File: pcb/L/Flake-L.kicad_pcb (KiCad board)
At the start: 2 copper layers, 139.2 x 114 mm, 62 parts, among them SW1 SW_Push, SW10 SW_Push, SW11 SW_Push, SW12 SW_Push, SW13 SW_Push, SW14 SW_Push, SW15 SW_Push, SW16 SW_Push, SW17 SW_Push, SW18 SW_Push, SW19 SW_Push, SW2 SW_Push, SW20 SW_Push, SW21 SW_Push, SW22 SW_Push, SW23 SW_Push, SW24 SW_Push, SW25 SW_Push, SW26 SW_Push, SW27 SW_Push, SW28 SW_Push, SW29 SW_Push, SW3 SW_Push, SW4 SW_Push, SW5 SW_Push, SW6 SW_Push, SW7 SW_Push, SW8 SW_Push, SW9 SW_Push, U1 XIAO-nRF52840-SMD

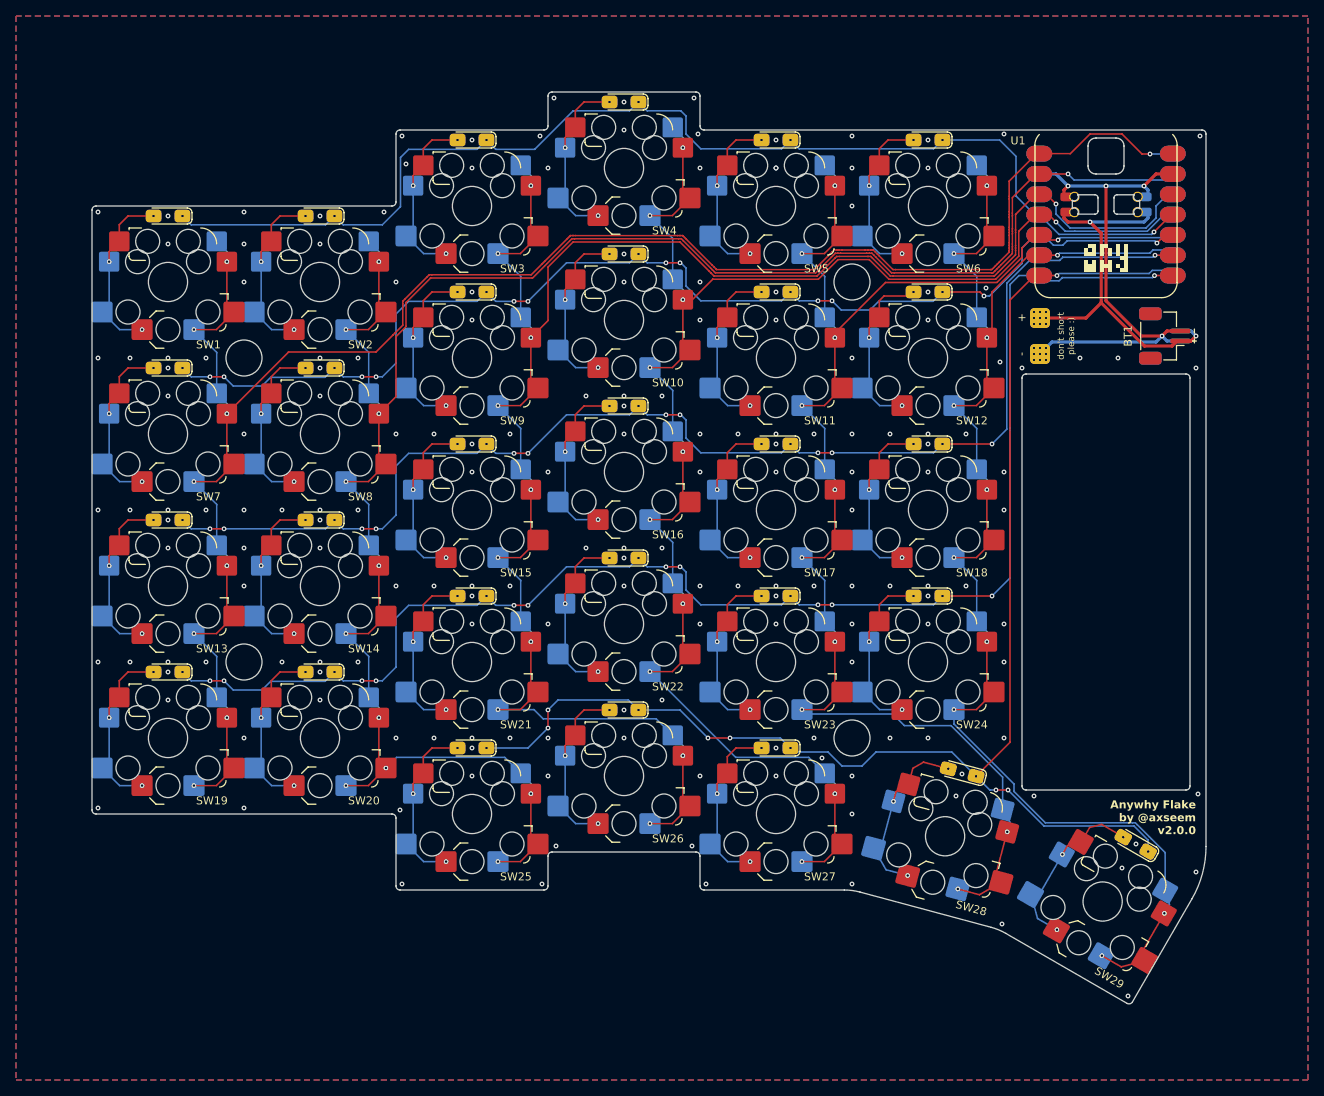
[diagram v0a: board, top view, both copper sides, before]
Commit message: fix(pcb): v2.0.1 boards with 1mm corner cuts and M,S reroute
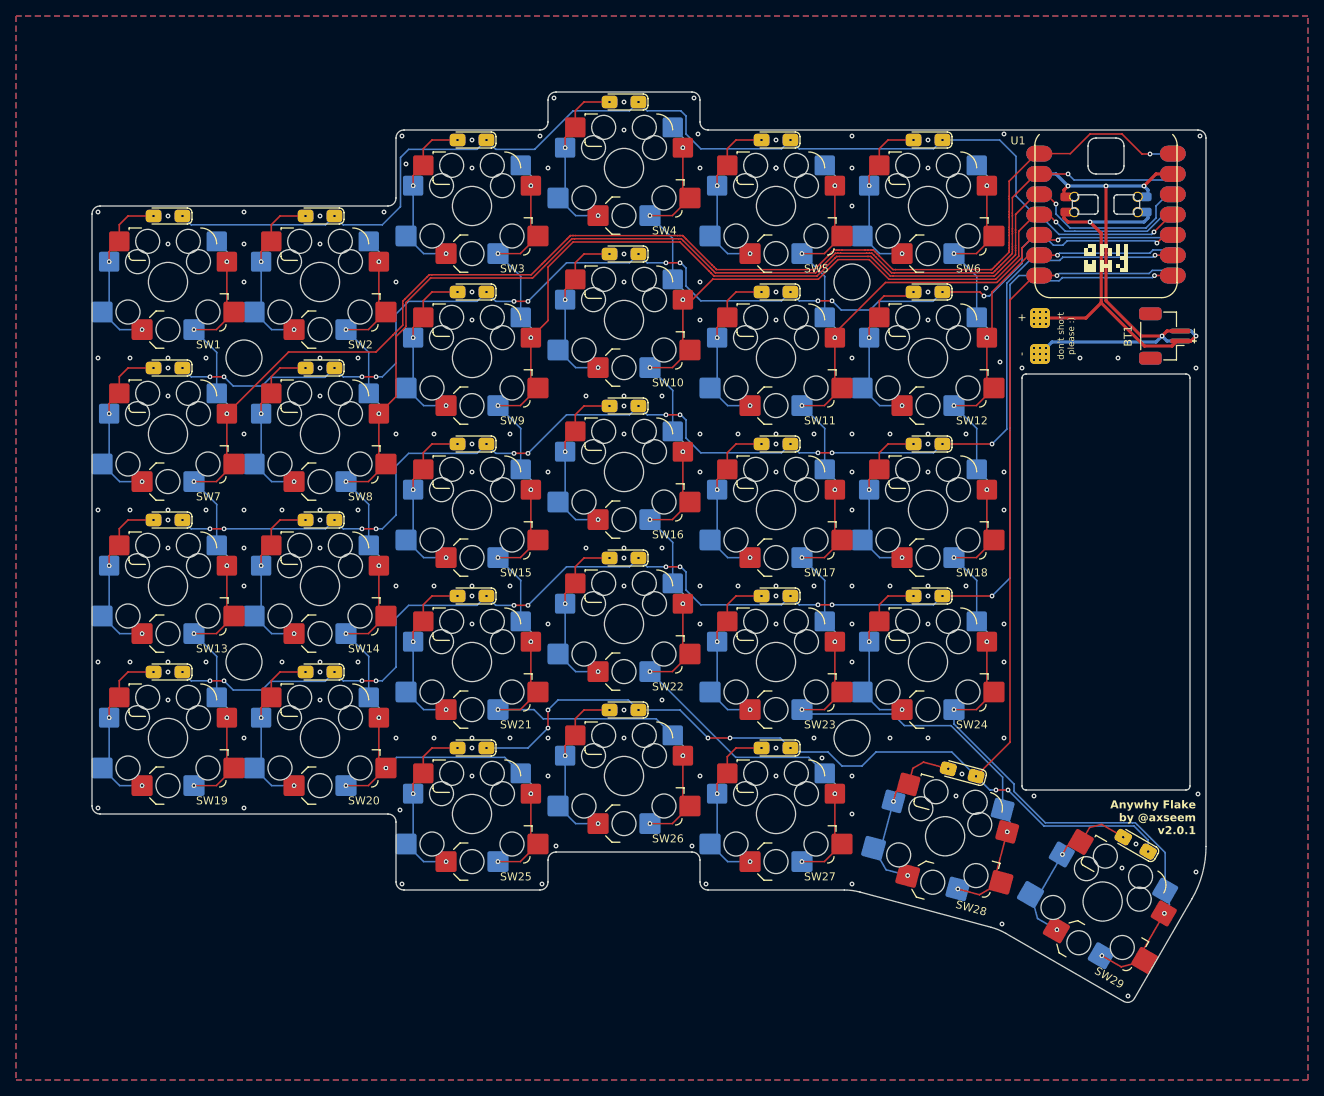
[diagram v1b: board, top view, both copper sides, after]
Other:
- board size 139.2 x 114 mm -> 139.2 x 113.8 mm
- board text added: "Anywhy Flake by @axseem v2.0.1"
- board text removed: "Anywhy Flake by @axseem v2.0.0"
